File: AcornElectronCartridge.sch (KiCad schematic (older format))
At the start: 8 parts, among them P11 CONN_01X08, P12 CONN_01X08, P13 CONN_01X06, P21 CONN_01X06, P22 CONN_01X08, P23 CONN_01X08

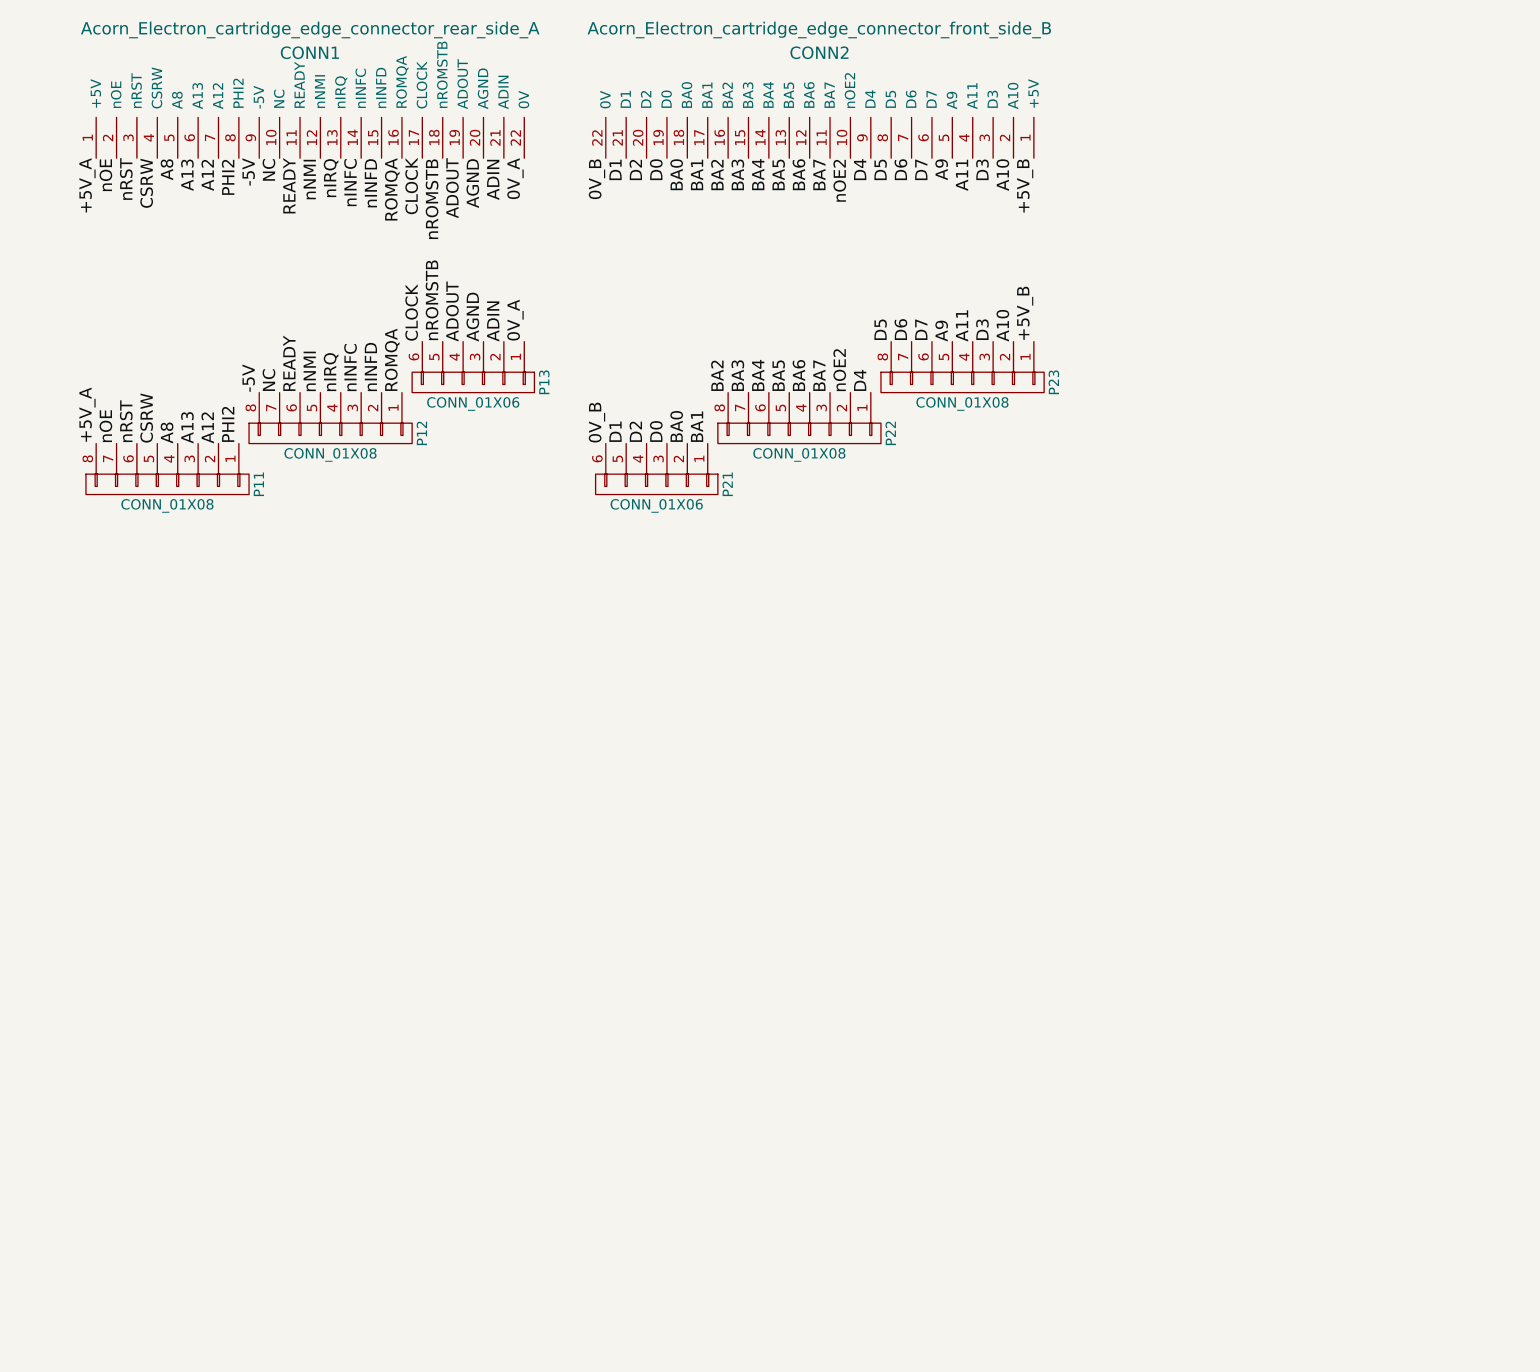
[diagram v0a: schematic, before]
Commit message: Finished the basic design.
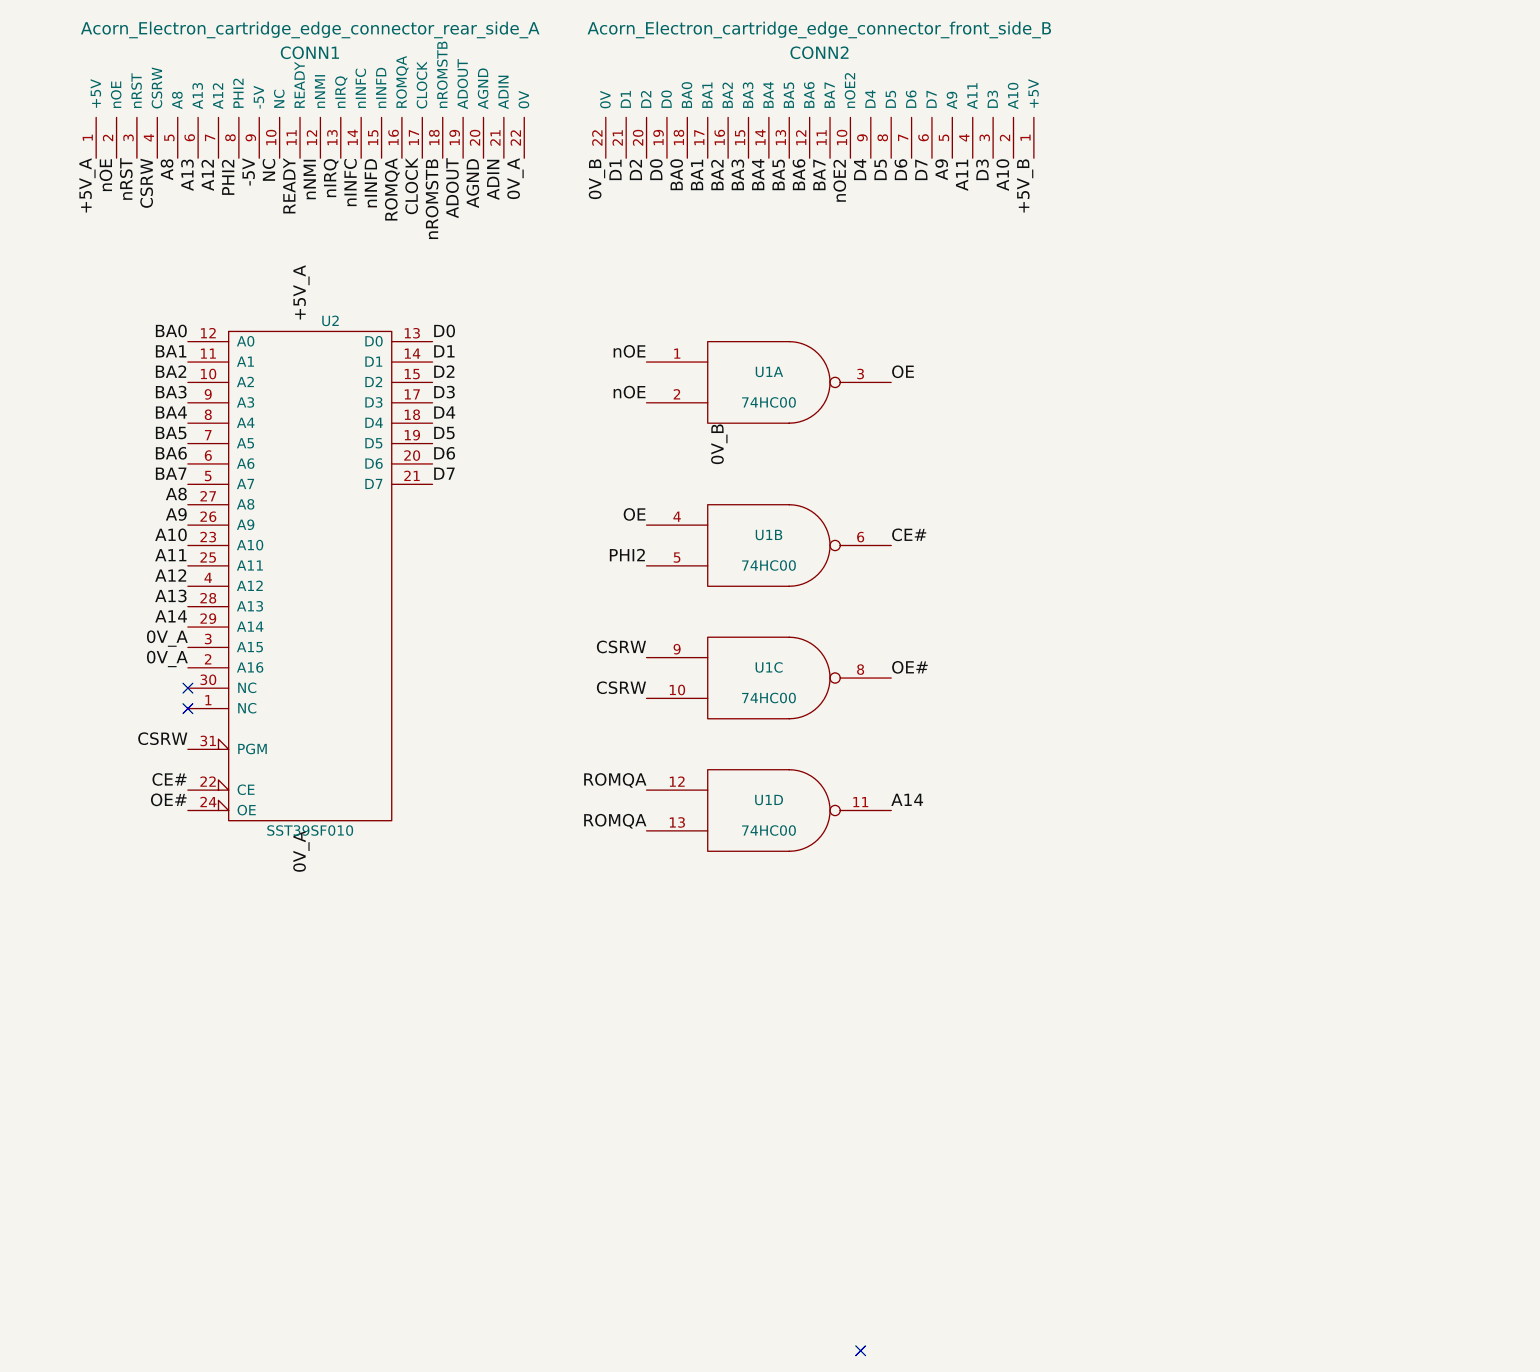
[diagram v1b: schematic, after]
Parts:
- removed P11, P12, P22, P23: CONN_01X08, Pin_Headers:Pin_Header_Straight_1x08, symbol CONN_01X08
- removed P13, P21: CONN_01X06, Pin_Headers:Pin_Header_Straight_1x06, symbol CONN_01X06
- added U1: 74HC00, Housings_DIP:DIP-14_W7.62mm, symbol 74HC00
- added U2: SST39SF010, Housings_DIP:DIP-32_W15.24mm, symbol SST39SF010
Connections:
- net 0V_B is gone; now on net GND: CONN2.22 (0V)
- net A10: now also U2.23 (A10)
- net A11: now also U2.25 (A11)
- net A12: now also U2.4 (A12)
- net A13: now also U2.28 (A13)
- net A8: now also U2.27 (A8)
- net A9: now also U2.26 (A9)
- net BA0: now also U2.12 (A0)
- net BA1: now also U2.11 (A1)
- net BA2: now also U2.10 (A2)
- net BA3: now also U2.9 (A3)
- net BA4: now also U2.8 (A4)
- net BA5: now also U2.7 (A5)
- net BA6: now also U2.6 (A6)
- net BA7: now also U2.5 (A7)
- net CSRW: now also U1.10, U1.9, U2.31 (PGM)
- net D0: now also U2.13 (D0)
- net D1: now also U2.14 (D1)
- net D2: now also U2.15 (D2)
- net D3: now also U2.17 (D3)
- net D4: now also U2.18 (D4)
- net D5: now also U2.19 (D5)
- net D6: now also U2.20 (D6)
- net D7: now also U2.21 (D7)
- net PHI2: now also U1.5
- net ROMQA: now also U1.12, U1.13
- net nOE: now also U1.1, U1.2
- net +5V_A renamed VCC
- net VCC: now also U1.14 (VCC), U1.14 (VCC), U1.14 (VCC), U1.14 (VCC), U2.32 (VCC)
- net 0V_A renamed GND
- net GND: now also U1.7 (GND), U1.7 (GND), U1.7 (GND), U1.7 (GND), U2.16 (GND), U2.2 (A16), U2.3 (A15)
- new net A14: U1.11, U2.29 (A14)
- new net CE#: U1.6, U2.22 (CE)
- new net OE: U1.3, U1.4
- new net OE#: U1.8, U2.24 (OE)
- no-connect marks 0 -> 3
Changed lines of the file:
@@
 encoding utf-8
 Sheet 1 1
-Title "Acorn Electron cartridge breakout"
-Date "2017-02-16"
+Title "Acorn Electron 32K EEPROM cartridge"
+Date "2017-10-02"
 Rev ""
 Comp ""
@@
 Comment2 "See: http://hgweb.boddie.org.uk/AcornElectronCartridge"
 Comment3 "Design licensed under the terms of the GNU General Public License version 3 or later."
-Comment4 "A prototyping/breakout cartridge for the Acorn Electron Plus 1 expansion unit."
+Comment4 "A 32K EEPROM cartridge for the Acorn Electron Plus 1 expansion unit."
 $EndDescr
 $Comp
@@
 	1    0    0    -1
 $EndComp
-$Comp
-L CONN_01X08 P11
-U 1 1 587CC917
-P 2050 3300
-F 0 "P11" H 2050 3750 50  0000 C CNN
-F 1 "CONN_01X08" V 2150 3300 50  0000 C CNN
-F 2 "Pin_Headers:Pin_Header_Straight_1x08" H 2050 3300 50  0001 C CNN
-F 3 "" H 2050 3300 50  0000 C CNN
-	1    2050 3300
-	0    1    1    0
-$EndComp
-$Comp
-L CONN_01X08 P12
-U 1 1 587CC9A6
-P 2850 3050
-F 0 "P12" H 2850 3500 50  0000 C CNN
-F 1 "CONN_01X08" V 2950 3050 50  0000 C CNN
-F 2 "Pin_Headers:Pin_Header_Straight_1x08" H 2850 3050 50  0001 C CNN
-F 3 "" H 2850 3050 50  0000 C CNN
-	1    2850 3050
-	0    1    1    0
-$EndComp
-$Comp
-L CONN_01X06 P13
-U 1 1 587CCAF1
-P 3550 2800
-F 0 "P13" H 3550 3150 50  0000 C CNN
-F 1 "CONN_01X06" V 3650 2800 50  0000 C CNN
-F 2 "Pin_Headers:Pin_Header_Straight_1x06" H 3550 2800 50  0001 C CNN
-F 3 "" H 3550 2800 50  0000 C CNN
-	1    3550 2800
-	0    1    1    0
-$EndComp
-$Comp
-L CONN_01X08 P22
-U 1 1 587CCB6A
-P 5150 3050
-F 0 "P22" H 5150 3500 50  0000 C CNN
-F 1 "CONN_01X08" V 5250 3050 50  0000 C CNN
-F 2 "Pin_Headers:Pin_Header_Straight_1x08" H 5150 3050 50  0001 C CNN
-F 3 "" H 5150 3050 50  0000 C CNN
-	1    5150 3050
-	0    1    1    0
-$EndComp
-$Comp
-L CONN_01X06 P21
-U 1 1 587CCBCE
-P 4450 3300
-F 0 "P21" H 4450 3650 50  0000 C CNN
-F 1 "CONN_01X06" V 4550 3300 50  0000 C CNN
-F 2 "Pin_Headers:Pin_Header_Straight_1x06" H 4450 3300 50  0001 C CNN
-F 3 "" H 4450 3300 50  0000 C CNN
-	1    4450 3300
-	0    1    1    0
-$EndComp
-$Comp
-L CONN_01X08 P23
-U 1 1 587CCC38
-P 5950 2800
-F 0 "P23" H 5950 3250 50  0000 C CNN
-F 1 "CONN_01X08" V 6050 2800 50  0000 C CNN
-F 2 "Pin_Headers:Pin_Header_Straight_1x08" H 5950 2800 50  0001 C CNN
-F 3 "" H 5950 2800 50  0000 C CNN
-	1    5950 2800
-	0    1    1    0
-$EndComp
-Text Label 1700 3100 1    60   ~ 0
-+5V_A
-Text Label 1800 3100 1    60   ~ 0
-nOE
-Text Label 1900 3100 1    60   ~ 0
-nRST
-Text Label 2000 3100 1    60   ~ 0
-CSRW
-Text Label 2100 3100 1    60   ~ 0
-A8
-Text Label 2200 3100 1    60   ~ 0
-A13
-Text Label 2300 3100 1    60   ~ 0
-A12
-Text Label 2400 3100 1    60   ~ 0
-PHI2
 Text Label 1700 1700 3    60   ~ 0
 +5V_A
@@
 Text Label 2400 1700 3    60   ~ 0
 PHI2
-Text Label 2500 2850 1    60   ~ 0
--5V
 Text Label 2500 1700 3    60   ~ 0
 -5V
-Text Label 2700 2850 1    60   ~ 0
-READY
 Text Label 2700 1700 3    60   ~ 0
 READY
-Text Label 2800 2850 1    60   ~ 0
-nNMI
 Text Label 2800 1700 3    60   ~ 0
 nNMI
-Text Label 2900 2850 1    60   ~ 0
-nIRQ
 Text Label 2900 1700 3    60   ~ 0
 nIRQ
-Text Label 3000 2850 1    60   ~ 0
-nINFC
 Text Label 3000 1700 3    60   ~ 0
 nINFC
-Text Label 3100 2850 1    60   ~ 0
-nINFD
 Text Label 3100 1700 3    60   ~ 0
 nINFD
-Text Label 3200 2850 1    60   ~ 0
-ROMQA
 Text Label 3200 1700 3    60   ~ 0
 ROMQA
-Text Label 3300 2600 1    60   ~ 0
-CLOCK
 Text Label 3300 1700 3    60   ~ 0
 CLOCK
-Text Label 3400 2600 1    60   ~ 0
-nROMSTB
 Text Label 3400 1700 3    60   ~ 0
 nROMSTB
-Text Label 3500 2600 1    60   ~ 0
-ADOUT
 Text Label 3500 1700 3    60   ~ 0
 ADOUT
-Text Label 3600 2600 1    60   ~ 0
-AGND
 Text Label 3600 1700 3    60   ~ 0
 AGND
-Text Label 3700 2600 1    60   ~ 0
-ADIN
 Text Label 3700 1700 3    60   ~ 0
 ADIN
-Text Label 3800 2600 1    60   ~ 0
-0V_A
 Text Label 3800 1700 3    60   ~ 0
 0V_A
-Text Label 4200 3100 1    60   ~ 0
-0V_B
 Text Label 4200 1700 3    60   ~ 0
 0V_B
-Text Label 4300 3100 1    60   ~ 0
-D1
 Text Label 4300 1700 3    60   ~ 0
 D1
-Text Label 4400 3100 1    60   ~ 0
-D2
 Text Label 4400 1700 3    60   ~ 0
 D2
-Text Label 4500 3100 1    60   ~ 0
-D0
 Text Label 4500 1700 3    60   ~ 0
 D0
-Text Label 4600 3100 1    60   ~ 0
-BA0
 Text Label 4600 1700 3    60   ~ 0
 BA0
-Text Label 4700 3100 1    60   ~ 0
-BA1
-Text Label 4800 2850 1    60   ~ 0
-BA2
 Text Label 4700 1700 3    60   ~ 0
 BA1
@@
 Text Label 4900 1700 3    60   ~ 0
 BA3
-Text Label 4900 2850 1    60   ~ 0
-BA3
-Text Label 5000 2850 1    60   ~ 0
-BA4
-Text Label 5100 2850 1    60   ~ 0
-BA5
-Text Label 5200 2850 1    60   ~ 0
-BA6
-Text Label 5300 2850 1    60   ~ 0
-BA7
 Text Label 5000 1700 3    60   ~ 0
 BA4
@@
 Text Label 5300 1700 3    60   ~ 0
 BA7
-Text Label 5400 2850 1    60   ~ 0
-nOE2
 Text Label 5400 1700 3    60   ~ 0
 nOE2
-Text Label 5500 2850 1    60   ~ 0
-D4
-Text Label 5600 2600 1    60   ~ 0
-D5
 Text Label 5500 1700 3    60   ~ 0
 D4
@@
 Text Label 5800 1700 3    60   ~ 0
 D7
-Text Label 5700 2600 1    60   ~ 0
-D6
-Text Label 5800 2600 1    60   ~ 0
-D7
-Text Label 5900 2600 1    60   ~ 0
-A9
 Text Label 5900 1700 3    60   ~ 0
 A9
-Text Label 6000 2600 1    60   ~ 0
-A11
 Text Label 6000 1700 3    60   ~ 0
 A11
-Text Label 6100 2600 1    60   ~ 0
-D3
 Text Label 6100 1700 3    60   ~ 0
 D3
-Text Label 6200 2600 1    60   ~ 0
-A10
 Text Label 6200 1700 3    60   ~ 0
 A10
-Text Label 6300 2600 1    60   ~ 0
-+5V_B
 Text Label 6300 1700 3    60   ~ 0
 +5V_B
-Text Label 2600 2850 1    60   ~ 0
-NC
 Text Label 2600 1700 3    60   ~ 0
 NC
+$Comp
+L 74HC00 U1
+U 1 1 59D29643
+P 5000 2800
+F 0 "U1" H 5000 2850 50  0000 C CNN
+F 1 "74HC00" H 5000 2700 50  0000 C CNN
+F 2 "Housings_DIP:DIP-14_W7.62mm" H 5000 2800 50  0001 C CNN
+F 3 "" H 5000 2800 50  0000 C CNN
+	1    5000 2800
+	1    0    0    -1
+$EndComp
+$Comp
+L 74HC00 U1
+U 2 1 59D29688
+P 5000 3600
+F 0 "U1" H 5000 3650 50  0000 C CNN
+F 1 "74HC00" H 5000 3500 50  0000 C CNN
+F 2 "Housings_DIP:DIP-14_W7.62mm" H 5000 3600 50  0001 C CNN
+F 3 "" H 5000 3600 50  0000 C CNN
+	2    5000 3600
+	1    0    0    -1
+$EndComp
+$Comp
+L 74HC00 U1
+U 3 1 59D296BF
+P 5000 4250
+F 0 "U1" H 5000 4300 50  0000 C CNN
+F 1 "74HC00" H 5000 4150 50  0000 C CNN
+F 2 "Housings_DIP:DIP-14_W7.62mm" H 5000 4250 50  0001 C CNN
+F 3 "" H 5000 4250 50  0000 C CNN
+	3    5000 4250
+	1    0    0    -1
+$EndComp
+$Comp
+L 74HC00 U1
+U 4 1 59D296F2
+P 5000 4900
+F 0 "U1" H 5000 4950 50  0000 C CNN
+F 1 "74HC00" H 5000 4800 50  0000 C CNN
+F 2 "Housings_DIP:DIP-14_W7.62mm" H 5000 4900 50  0001 C CNN
+F 3 "" H 5000 4900 50  0000 C CNN
+	4    5000 4900
+	1    0    0    -1
+$EndComp
+Text Label 4400 2700 2    60   ~ 0
+nOE
+Text Label 4400 2900 2    60   ~ 0
+nOE
+Text Label 5600 2800 0    60   ~ 0
+OE
+Text Label 4400 3500 2    60   ~ 0
+OE
+Text Label 4400 3700 2    60   ~ 0
+PHI2
+Text Label 5600 3600 0    60   ~ 0
+CE#
+Text Label 4400 4150 2    60   ~ 0
+CSRW
+Text Label 4400 4350 2    60   ~ 0
+CSRW
+Text Label 5600 4250 0    60   ~ 0
+OE#
+Text Label 4400 4800 2    60   ~ 0
+ROMQA
+Text Label 4400 5000 2    60   ~ 0
+ROMQA
+Text Label 5600 4900 0    60   ~ 0
+A14
+$Comp
+L SST39SF010 U2
+U 1 1 59D2A464
+P 2750 3800
+F 0 "U2" H 2850 5100 50  0000 C CNN
+F 1 "SST39SF010" H 2750 2600 50  0000 C CNN
+F 2 "Housings_DIP:DIP-32_W15.24mm" H 2750 4100 50  0001 C CNN
+F 3 "" H 2750 4100 50  0000 C CNN
+	1    2750 3800
+	1    0    0    -1
+$EndComp
+Text Label 2150 4800 2    60   ~ 0
+CE#
+Text Label 2150 4900 2    60   ~ 0
+OE#
+Text Label 3350 3300 0    60   ~ 0
+D7
+Text Label 3350 3200 0    60   ~ 0
+D6
+Text Label 3350 3100 0    60   ~ 0
+D5
+Text Label 3350 3000 0    60   ~ 0
+D4
+Text Label 3350 2900 0    60   ~ 0
+D3
+Text Label 3350 2800 0    60   ~ 0
+D2
+Text Label 3350 2700 0    60   ~ 0
+D1
+Text Label 3350 2600 0    60   ~ 0
+D0
+Text Label 2150 2600 2    60   ~ 0
+BA0
+Text Label 2150 2700 2    60   ~ 0
+BA1
+Text Label 2150 2800 2    60   ~ 0
+BA2
+Text Label 2150 2900 2    60   ~ 0
+BA3
+Text Label 2150 3000 2    60   ~ 0
+BA4
+Text Label 2150 3100 2    60   ~ 0
+BA5
+Text Label 2150 3200 2    60   ~ 0
+BA6
+Text Label 2150 3300 2    60   ~ 0
+BA7
+Text Label 2150 3400 2    60   ~ 0
+A8
+Text Label 2150 3500 2    60   ~ 0
+A9
+Text Label 2150 3600 2    60   ~ 0
+A10
+Text Label 2150 3700 2    60   ~ 0
+A11
+Text Label 2150 3800 2    60   ~ 0
+A12
+Text Label 2150 3900 2    60   ~ 0
+A13
+Text Label 2150 4000 2    60   ~ 0
+A14
+Text Label 2150 4100 2    60   ~ 0
+0V_A
+Text Label 2150 4200 2    60   ~ 0
+0V_A
+Text Label 2750 2500 1    60   ~ 0
++5V_A
+Text Label 2750 5000 3    60   ~ 0
+0V_A
+NoConn ~ 2150 4300
+NoConn ~ 2150 4400
+NoConn ~ 5450 7550
+Text Label 4800 3000 3    60   ~ 0
+0V_B
+Text Label 2150 4600 2    60   ~ 0
+CSRW
 $EndSCHEMATC
